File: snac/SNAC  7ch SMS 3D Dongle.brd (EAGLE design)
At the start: 37.3 x 23.8 mm, 21 parts, among them IC1 4030D, IC2 4030D, K2 692112030100, Q9 BC849SMD, X2 STEREOJACK

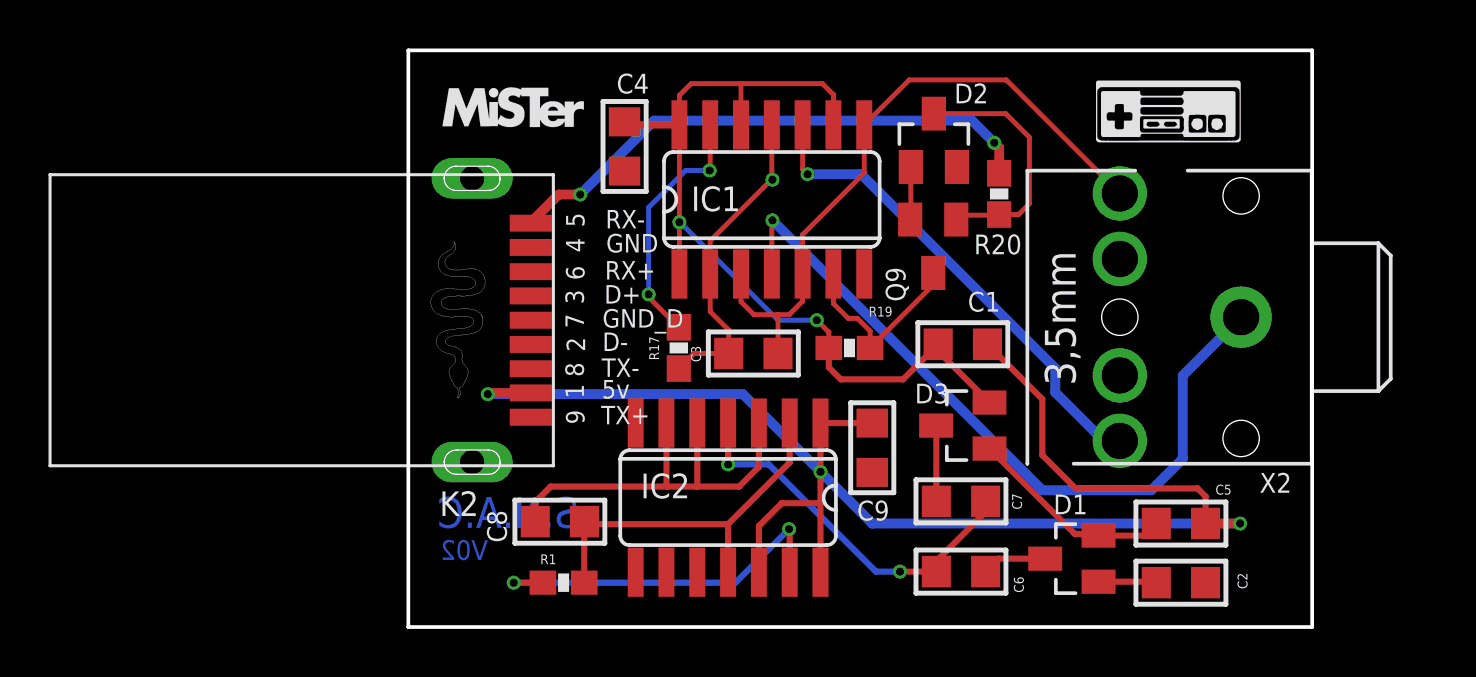
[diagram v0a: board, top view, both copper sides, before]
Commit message: Changed to a MAX660 charge pump on the JST DB9 3D Glasses board
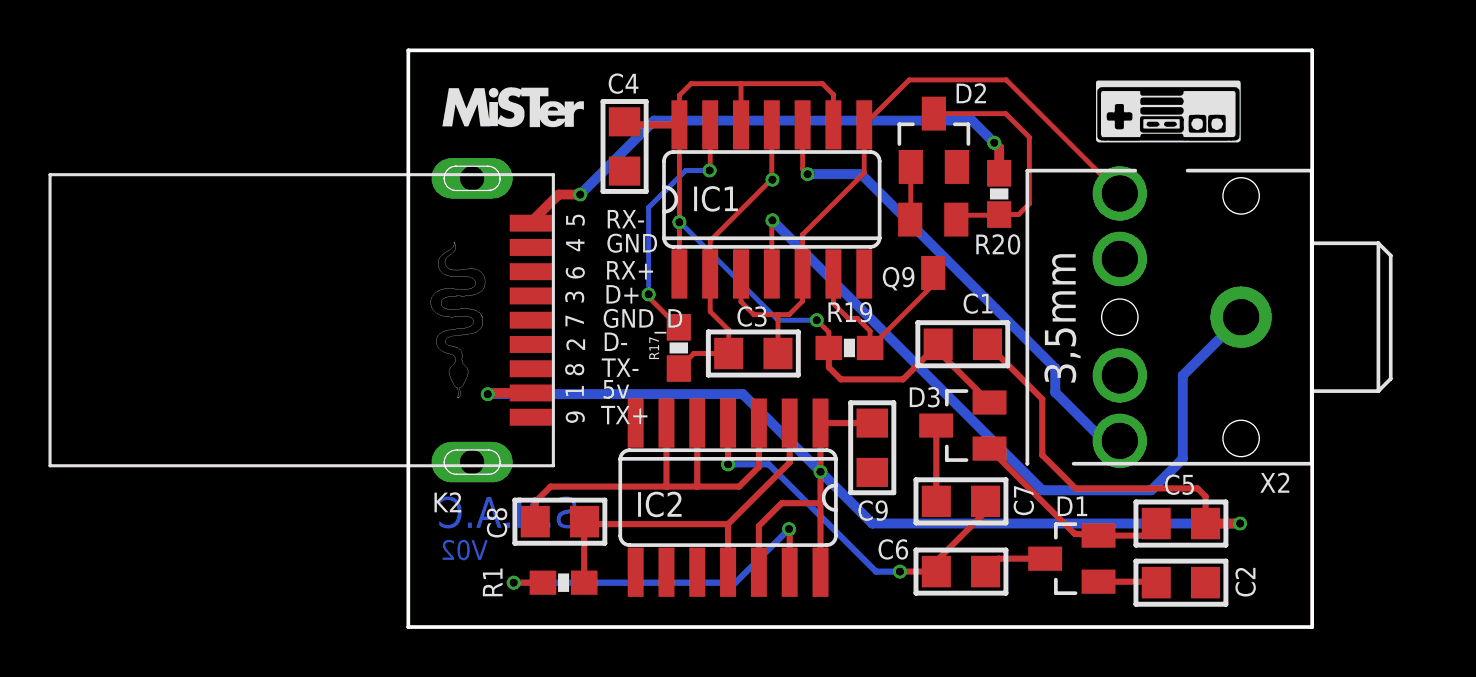
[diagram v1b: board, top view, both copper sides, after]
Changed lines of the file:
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@@
 <elements>
 <element name="K2" library="Wuerth_Elektronik_eiCan_Communication_Connectors_STENCIL" package="692112030100" value="692112030100" x="6.3754" y="13.9446" smashed="yes" rot="R90">
-<attribute name="NAME" x="2.5804" y="5.8716" size="1.016" layer="25"/>
+<attribute name="NAME" x="2.2756" y="6.024" size="0.8128" layer="25"/>
 </element>
 <element name="IC1" library="40xx" package="SO14" value="4030D" x="16.2814" y="18.923" smashed="yes">
@@
 </element>
 <element name="C3" library="rc-master-smd" package="C0805" value="10nF" x="15.5194" y="12.573" smashed="yes">
-<attribute name="NAME" x="13.3604" y="12.2174" size="0.4064" layer="25" ratio="18" rot="R90"/>
+<attribute name="NAME" x="14.8082" y="13.6906" size="0.8128" layer="25" ratio="18"/>
 <attribute name="VALUE" x="13.7414" y="10.795" size="0.4064" layer="27" ratio="10"/>
 </element>
 <element name="Q9" library="transistor-npn" library_urn="urn:adsk.eagle:library:398" package="SOT23-BEC" package3d_urn="urn:adsk.eagle:package:28990/2" value="BC849SMD" x="22.9362" y="16.9926" smashed="yes" rot="R180">
-<attribute name="NAME" x="21.7932" y="14.7066" size="0.8128" layer="25" rot="R90"/>
+<attribute name="NAME" x="20.8026" y="15.3162" size="0.8128" layer="25"/>
 <attribute name="VALUE" x="24.8412" y="20.1676" size="1.27" layer="27" rot="R180"/>
 </element>
 <element name="R19" library="SparkFun" package="0603-RES" value="10K" x="19.4818" y="12.8016" smashed="yes">
-<attribute name="NAME" x="20.2692" y="14.097" size="0.4064" layer="25"/>
+<attribute name="NAME" x="18.5166" y="13.8684" size="0.8128" layer="25"/>
 <attribute name="VALUE" x="18.4658" y="11.6586" size="0.4064" layer="27" font="vector"/>
 </element>
@@
 </element>
 <element name="C4" library="rc-master-smd" package="C0805" value="22uF" x="10.2108" y="21.1074" smashed="yes" rot="R270">
-<attribute name="NAME" x="9.8806" y="23.2918" size="0.8128" layer="25" ratio="18"/>
+<attribute name="NAME" x="9.4996" y="23.2918" size="0.8128" layer="25" ratio="18"/>
 <attribute name="VALUE" x="8.4328" y="22.8854" size="0.4064" layer="27" ratio="10" rot="R270"/>
 </element>
@@
 </element>
 <element name="D1" library="diode" library_urn="urn:adsk.eagle:library:210" package="SOT23" package3d_urn="urn:adsk.eagle:package:43389/2" value="BAS40-04" x="28.6512" y="4.1148" smashed="yes" rot="R90">
-<attribute name="NAME" x="27.8892" y="5.9436" size="0.8128" layer="25"/>
+<attribute name="NAME" x="27.9654" y="5.8674" size="0.8128" layer="25"/>
 <attribute name="POPULARITY" value="6" x="28.6512" y="4.1148" size="1.778" layer="27" rot="R90" display="off"/>
 <attribute name="VALUE" x="31.8262" y="2.2098" size="1.27" layer="27" rot="R90"/>
 </element>
 <element name="D3" library="diode" library_urn="urn:adsk.eagle:library:210" package="SOT23" package3d_urn="urn:adsk.eagle:package:43389/2" value="BAS40-04" x="24.1554" y="9.6012" smashed="yes" rot="R90">
-<attribute name="NAME" x="22.1742" y="10.5156" size="0.8128" layer="25"/>
+<attribute name="NAME" x="21.8694" y="10.3632" size="0.8128" layer="25"/>
 <attribute name="POPULARITY" value="6" x="24.1554" y="9.6012" size="1.778" layer="27" rot="R90" display="off"/>
 <attribute name="VALUE" x="27.3304" y="7.6962" size="1.27" layer="27" rot="R90"/>
 </element>
 <element name="C1" library="rc-master-smd" package="C0805" value="2.2uF" x="24.1554" y="12.954" smashed="yes">
-<attribute name="NAME" x="24.3586" y="14.3002" size="0.8128" layer="25" ratio="18"/>
+<attribute name="NAME" x="24.13" y="14.224" size="0.8128" layer="25" ratio="18"/>
 <attribute name="VALUE" x="22.3774" y="11.176" size="0.4064" layer="27" ratio="10"/>
 </element>
 <element name="C2" library="rc-master-smd" package="C0805" value="2.2uF" x="33.147" y="3.1242" smashed="yes">
-<attribute name="NAME" x="35.4838" y="3.5306" size="0.4064" layer="25" ratio="18" rot="R270"/>
+<attribute name="NAME" x="35.4076" y="3.8354" size="0.8128" layer="25" ratio="18" rot="R270"/>
 <attribute name="VALUE" x="31.369" y="1.3462" size="0.4064" layer="27" ratio="10"/>
 </element>
 <element name="C5" library="rc-master-smd" package="C0805" value="2.2uF" x="33.147" y="5.5626" smashed="yes">
-<attribute name="NAME" x="34.5694" y="6.7564" size="0.4064" layer="25" ratio="18"/>
+<attribute name="NAME" x="32.4358" y="6.7564" size="0.8128" layer="25" ratio="18"/>
 <attribute name="VALUE" x="31.369" y="3.7846" size="0.4064" layer="27" ratio="10"/>
 </element>
 <element name="C6" library="rc-master-smd" package="C0805" value="2.2uF" x="24.0792" y="3.5814" smashed="yes">
-<attribute name="NAME" x="26.2636" y="3.3782" size="0.4064" layer="25" ratio="18" rot="R270"/>
+<attribute name="NAME" x="20.6248" y="4.0894" size="0.8128" layer="25" ratio="18"/>
 <attribute name="VALUE" x="22.3012" y="1.8034" size="0.4064" layer="27" ratio="10"/>
 </element>
 <element name="C7" library="rc-master-smd" package="C0805" value="2.2uF" x="24.0792" y="6.477" smashed="yes" rot="R180">
-<attribute name="NAME" x="26.1874" y="6.8072" size="0.4064" layer="25" ratio="18" rot="R270"/>
+<attribute name="NAME" x="26.2636" y="7.1882" size="0.8128" layer="25" ratio="18" rot="R270"/>
 <attribute name="VALUE" x="25.8572" y="8.255" size="0.4064" layer="27" ratio="10" rot="R180"/>
 </element>
 <element name="IC2" library="40xx" package="SO14" value="4030D" x="14.478" y="6.6294" smashed="yes" rot="R180">
-<attribute name="NAME" x="10.8712" y="6.604" size="1.016" layer="25" ratio="10"/>
+<attribute name="NAME" x="10.6426" y="5.842" size="1.016" layer="25" ratio="10"/>
 <attribute name="VALUE" x="18.034" y="7.2644" size="1.27" layer="27" ratio="10" rot="R180"/>
 </element>
 <element name="R1" library="SparkFun" package="0603-RES" value="75K" x="7.6962" y="3.1242" smashed="yes">
-<attribute name="NAME" x="6.731" y="3.8862" size="0.4064" layer="25"/>
+<attribute name="NAME" x="5.1816" y="2.4638" size="0.8128" layer="25" rot="R90"/>
 <attribute name="VALUE" x="6.6802" y="1.9812" size="0.4064" layer="27" font="vector"/>
 </element>
 <element name="C8" library="rc-master-smd" package="C0805" value="10nF" x="7.5438" y="5.6388" smashed="yes" rot="R180">
-<attribute name="NAME" x="5.3594" y="4.7752" size="0.8128" layer="25" ratio="18" rot="R90"/>
+<attribute name="NAME" x="5.3594" y="4.9276" size="0.8128" layer="25" ratio="18" rot="R90"/>
 <attribute name="VALUE" x="9.3218" y="7.4168" size="0.4064" layer="27" ratio="10" rot="R180"/>
 </element>

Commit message: SMS 3D dongle charge pump and BOM updated
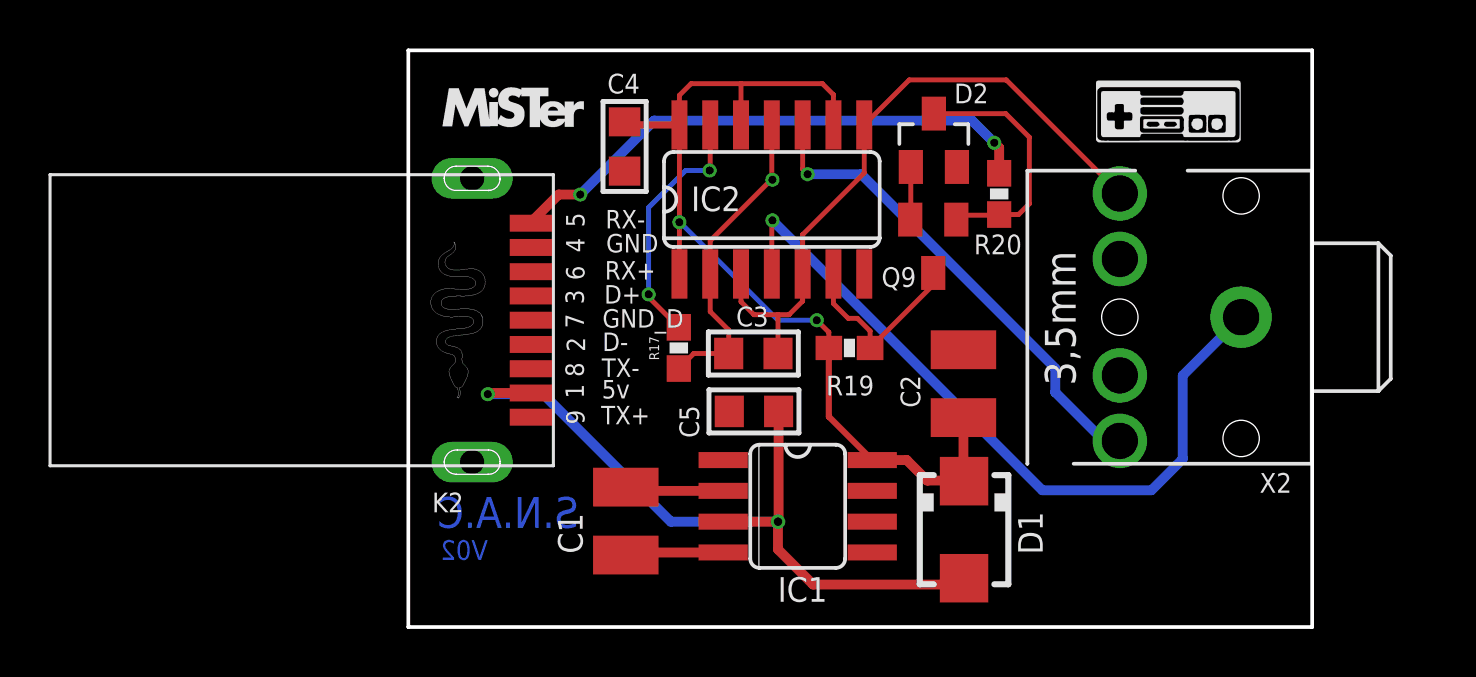
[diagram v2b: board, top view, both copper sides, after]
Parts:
- removed C6, C7: 2.2uF, rc-master-smd:C0805
- removed C8: 10nF, rc-master-smd:C0805
- removed C9: 22uF, rc-master-smd:C0805
- removed D3: BAS40-04, diode:SOT23
- removed R1: 75K, SparkFun:0603-RES
- C1, C2: value 2.2uF -> 100uF; device rc-master-smd:C0805 -> rcl:C1210
- C5: value 2.2uF -> 22uF
- D1: value BAS40-04 -> MBRA340T3; device diode:SOT23 -> diode:SMA
- IC1: value 4030D -> MAX660CPACS; device 40xx:SO14 -> maxim:SO08
- moved C5 18.2 mm to (15.5, 10.2), turned to 180 degrees
- moved C1 15.7 mm to (10.3, 5.66), turned to 270 degrees
- moved IC1 12.7 mm to (17.3, 6.27), turned to 270 degrees
- moved IC2 12.4 mm to (16.3, 18.9), turned to 0 degrees
- moved C2 12.2 mm to (24.2, 11.3), turned to 90 degrees
- moved D1 4.60 mm to (24.2, 5.31), turned to 270 degrees
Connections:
- removed net N$11: C7.2, D3.3
- removed net N$12: C6.2, D1.3
- removed net N$16: C8.1, IC2.11, IC2.2, R1.2
- removed net N$17: IC2.13, R1.1
- removed net N$6: C5.1, D1.2, D3.1
- removed net N$7: C6.1, C7.1, IC2.4
- removed net N$8: C2.1, D1.1
- removed net N$9: C8.2, IC2.3, IC2.5, IC2.6
- new net N$25: C1.1, IC1.2
- new net N$26: C1.2, IC1.4
- net 10V: now also C2.1, D1.C, IC1.8, IC2.1, IC2.12, IC2.14, IC2.9; no longer C1.1, D3.2, IC1.1, IC1.12, IC1.14, IC1.9
- net GND: now also C5.2, IC1.5, IC1.6; no longer C9.2, IC1.7, IC2.8, IC2.9
- net HV: now also C5.1, D1.A, IC1.3; no longer C1.2, C5.2, C9.1, IC2.1, IC2.12, IC2.14
- net N$10: now also IC2.13; no longer IC1.13
- net N$13: now also IC2.6; no longer IC1.6
- net N$5: now also IC2.11, IC2.2; no longer IC1.11, IC1.2
- net RING: now also IC2.10; no longer IC1.10
- net SLEEVE: now also IC2.4; no longer IC1.4
- net TIP: now also IC2.3, IC2.5, IC2.8; no longer IC1.3, IC1.5, IC1.8
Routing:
- net HV: track 63.6 -> 32.3 mm, vias 3 -> 2
- net N$9: track 17.7 -> 0.00 mm
- net N$7: track 15.9 -> 0.00 mm, vias 2 -> 0
- net N$16: track 15.7 -> 0.00 mm
- net N$17: track 15.3 -> 0.00 mm, vias 2 -> 0
- net N$6: track 8.54 -> 0.00 mm
- net N$25: track 0.00 -> 4.03 mm
- net N$26: track 0.00 -> 4.02 mm
- net N$11: track 3.13 -> 0.00 mm
- net 10V: track 37.5 -> 40.2 mm
- net N$12: track 2.68 -> 0.00 mm
- net N$8: track 2.40 -> 0.00 mm

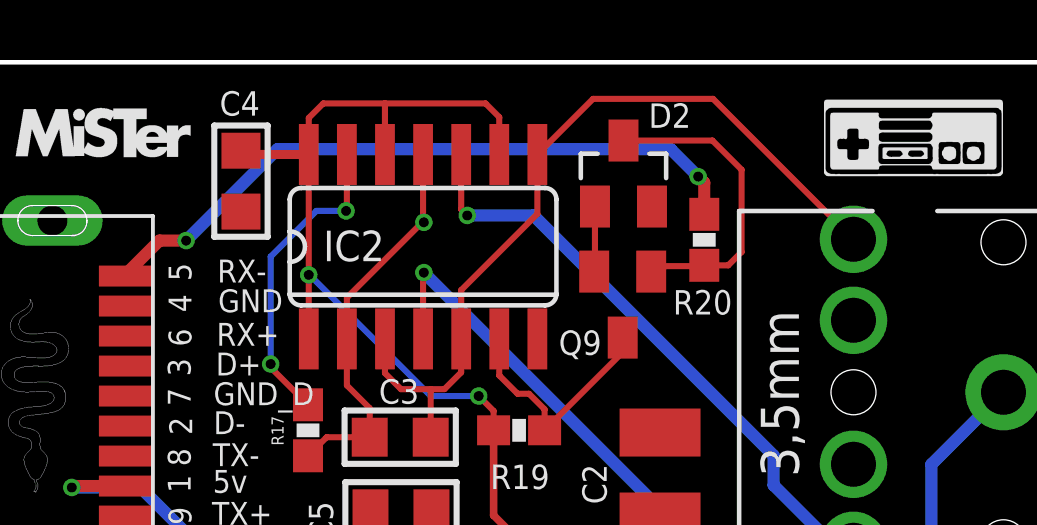
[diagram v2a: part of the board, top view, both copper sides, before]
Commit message: Removed unneeded diode from the SMS 3D dongle + BOM
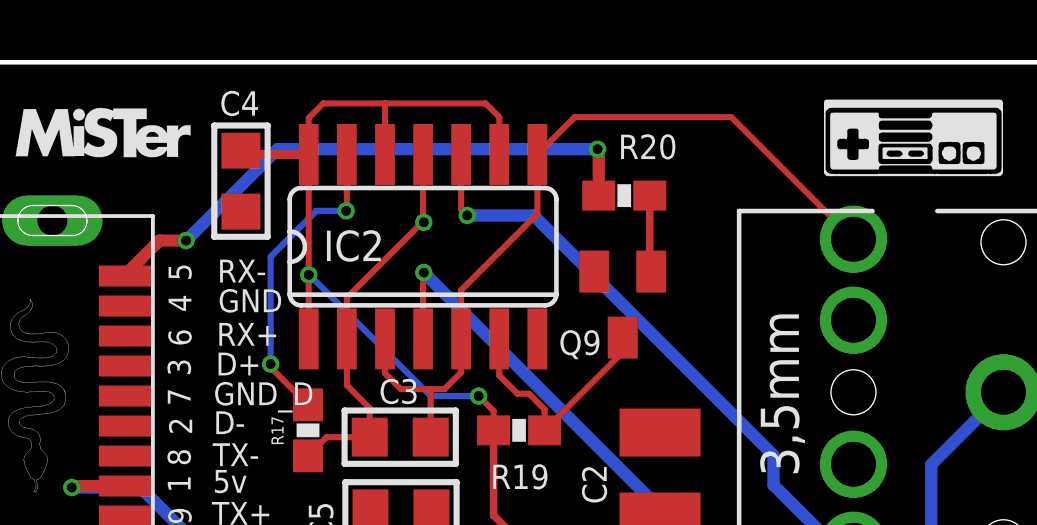
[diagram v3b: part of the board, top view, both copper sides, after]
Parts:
- removed D2: BAT54, diode:SOT23
- moved R20 3.05 mm to (23.0, 20.6), turned to 0 degrees
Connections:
- net GND: no longer D2.1
- net N$14: no longer D2.3
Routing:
- net N$14: track 10.4 -> 2.74 mm
- net LV6: track 22.6 -> 19.1 mm
- net GND: track 2.52 -> 0.53 mm
- net TIP: track 27.3 -> 26.8 mm
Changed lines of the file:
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@@
 <attribute name="VALUE" x="18.4658" y="11.6586" size="0.4064" layer="27" font="vector"/>
 </element>
-<element name="R20" library="SparkFun" package="0603-RES" value="10K" x="25.654" y="19.1516" smashed="yes" rot="R270">
-<attribute name="NAME" x="24.6126" y="16.6624" size="0.8128" layer="25"/>
-<attribute name="VALUE" x="24.511" y="20.1676" size="0.4064" layer="27" font="vector" rot="R270"/>
-</element>
-<element name="D2" library="diode" library_urn="urn:adsk.eagle:library:210" package="SOT23" package3d_urn="urn:adsk.eagle:package:43389/2" value="BAT54" x="22.9616" y="21.3614" smashed="yes">
-<attribute name="NAME" x="23.7998" y="22.8854" size="0.8128" layer="25"/>
-<attribute name="VALUE" x="21.0566" y="18.1864" size="1.27" layer="27"/>
+<element name="R20" library="SparkFun" package="0603-RES" value="10K" x="22.987" y="20.6248" smashed="yes">
+<attribute name="NAME" x="22.7838" y="21.844" size="0.8128" layer="25"/>
+<attribute name="VALUE" x="21.971" y="19.4818" size="0.4064" layer="27" font="vector"/>
 </element>
 <element name="C4" library="rc-master-smd" package="C0805" value="22uF" x="10.2108" y="21.1074" smashed="yes" rot="R270">
@@
 <contactref element="IC2" pad="7"/>
 <contactref element="Q9" pad="E"/>
-<contactref element="D2" pad="1"/>
 <wire x1="21.9862" y1="17.7444" x2="21.9862" y2="18.0926" width="0.2032" layer="1"/>
 <wire x1="21.9862" y1="18.0926" x2="22.0116" y2="18.2704" width="0.2032" layer="1"/>
-<wire x1="22.0116" y1="18.2704" x2="22.0116" y2="20.2614" width="0.2032" layer="1"/>
 <contactref element="C4" pad="2"/>
 <polygon width="0.1524" layer="1">
@@
 <wire x1="6.3754" y1="18.0086" x2="6.3754" y2="17.9446" width="0.1778" layer="1"/>
 <contactref element="R20" pad="1"/>
-<wire x1="25.654" y1="20.0016" x2="25.654" y2="21.0566" width="0.4064" layer="1"/>
-<wire x1="25.654" y1="21.0566" x2="25.4508" y2="21.2598" width="0.4064" layer="1"/>
-<via x="25.4508" y="21.2598" extent="1-16" drill="0.3302"/>
-<wire x1="25.4508" y1="21.2598" x2="24.5364" y2="22.1742" width="0.4064" layer="16"/>
-<wire x1="24.5364" y1="22.1742" x2="11.43" y2="22.1742" width="0.4064" layer="16"/>
-<wire x1="11.43" y1="22.1742" x2="8.382" y2="19.1262" width="0.4064" layer="16"/>
+<via x="22.098" y="22.1742" extent="1-16" drill="0.3302"/>
+<wire x1="8.382" y1="19.1262" x2="11.43" y2="22.1742" width="0.4064" layer="16"/>
 <via x="8.382" y="19.1262" extent="1-16" drill="0.3302"/>
 <wire x1="8.382" y1="19.1262" x2="7.493" y2="19.1262" width="0.4064" layer="1"/>
 <wire x1="7.493" y1="19.1262" x2="6.3754" y2="18.0086" width="0.4064" layer="1"/>
+<wire x1="11.43" y1="22.1742" x2="22.098" y2="22.1742" width="0.4064" layer="16"/>
+<wire x1="22.137" y1="20.6248" x2="22.137" y2="22.1352" width="0.4064" layer="1"/>
+<wire x1="22.137" y1="22.1352" x2="22.098" y2="22.1742" width="0.4064" layer="1"/>
 </signal>
 <signal name="LV7">
@@
 <contactref element="C3" pad="2"/>
 <contactref element="X2" pad="5"/>
-<wire x1="20.0914" y1="21.9964" x2="21.9456" y2="23.8506" width="0.2032" layer="1"/>
 <wire x1="15.0114" y1="15.8496" x2="15.0114" y2="14.7066" width="0.2032" layer="1"/>
 <wire x1="17.5514" y1="14.732" x2="17.5514" y2="15.8496" width="0.2032" layer="1"/>
@@
 <wire x1="17.5514" y1="17.4752" x2="20.0914" y2="20.0152" width="0.2032" layer="1"/>
 <wire x1="16.5354" y1="12.573" x2="16.5354" y2="14.1732" width="0.2032" layer="1"/>
-<wire x1="21.9456" y1="23.8506" x2="25.948" y2="23.8506" width="0.2032" layer="1"/>
-<wire x1="25.948" y1="23.8506" x2="30.6286" y2="19.17" width="0.2032" layer="1"/>
+<wire x1="30.6286" y1="19.17" x2="26.5576" y2="23.241" width="0.2032" layer="1"/>
+<wire x1="21.336" y1="23.241" x2="20.0914" y2="21.9964" width="0.2032" layer="1"/>
+<wire x1="26.5576" y1="23.241" x2="21.336" y2="23.241" width="0.2032" layer="1"/>
 </signal>
 <signal name="SLEEVE">
@@
 <contactref element="R20" pad="2"/>
 <contactref element="Q9" pad="B"/>
-<contactref element="D2" pad="3"/>
 <wire x1="23.8862" y1="18.0926" x2="23.9156" y2="18.2744" width="0.2032" layer="1"/>
-<wire x1="23.9156" y1="18.2744" x2="25.6268" y2="18.2744" width="0.2032" layer="1"/>
-<wire x1="25.6268" y1="18.2744" x2="25.654" y2="18.3016" width="0.2032" layer="1"/>
-<wire x1="25.9256" y1="22.4614" x2="26.8986" y2="21.4884" width="0.2032" layer="1"/>
-<wire x1="26.8986" y1="21.4884" x2="26.8986" y2="18.7452" width="0.2032" layer="1"/>
-<wire x1="26.455" y1="18.3016" x2="25.654" y2="18.3016" width="0.2032" layer="1"/>
-<wire x1="22.9616" y1="22.4614" x2="25.9256" y2="22.4614" width="0.2032" layer="1"/>
-<wire x1="26.8986" y1="18.7452" x2="26.455" y2="18.3016" width="0.2032" layer="1"/>
+<wire x1="23.8862" y1="18.0926" x2="23.837" y2="18.1418" width="0.254" layer="1"/>
+<wire x1="23.837" y1="18.1418" x2="23.837" y2="20.6248" width="0.254" layer="1"/>
 </signal>
 <signal name="10V">
